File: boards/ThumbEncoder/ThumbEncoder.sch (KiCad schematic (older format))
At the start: 7 parts, among them P1 CONN_5X2, P2 CONN_5X2, P3 CONN_5X2, P4 CONN_1

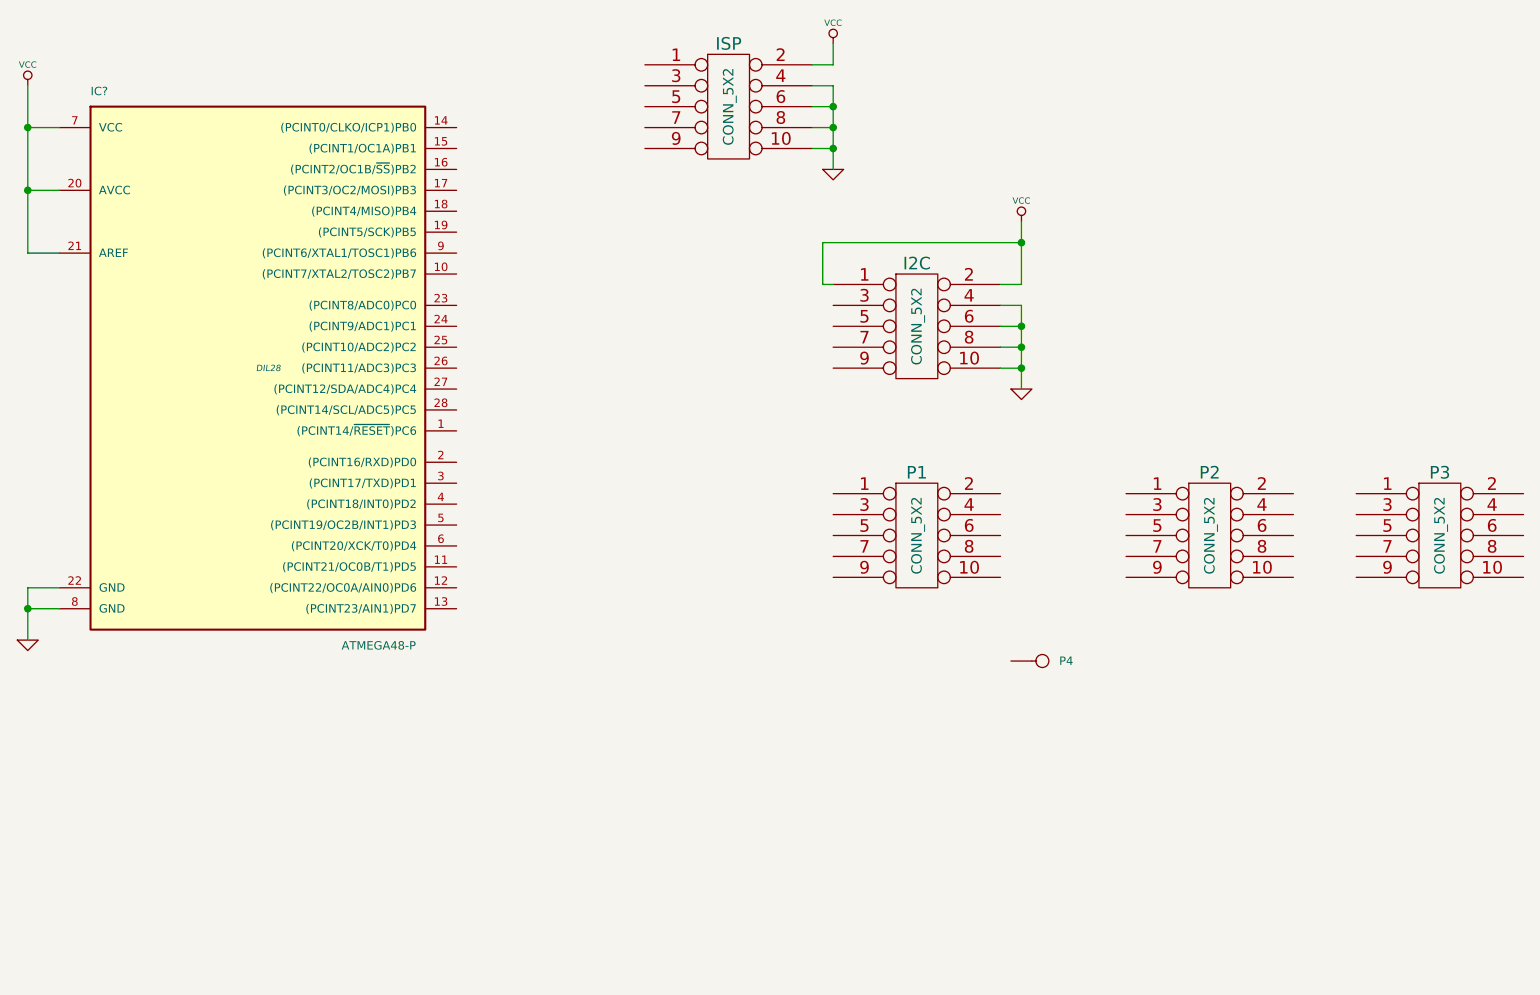
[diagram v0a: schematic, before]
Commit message: First version of thumb encoder schematics
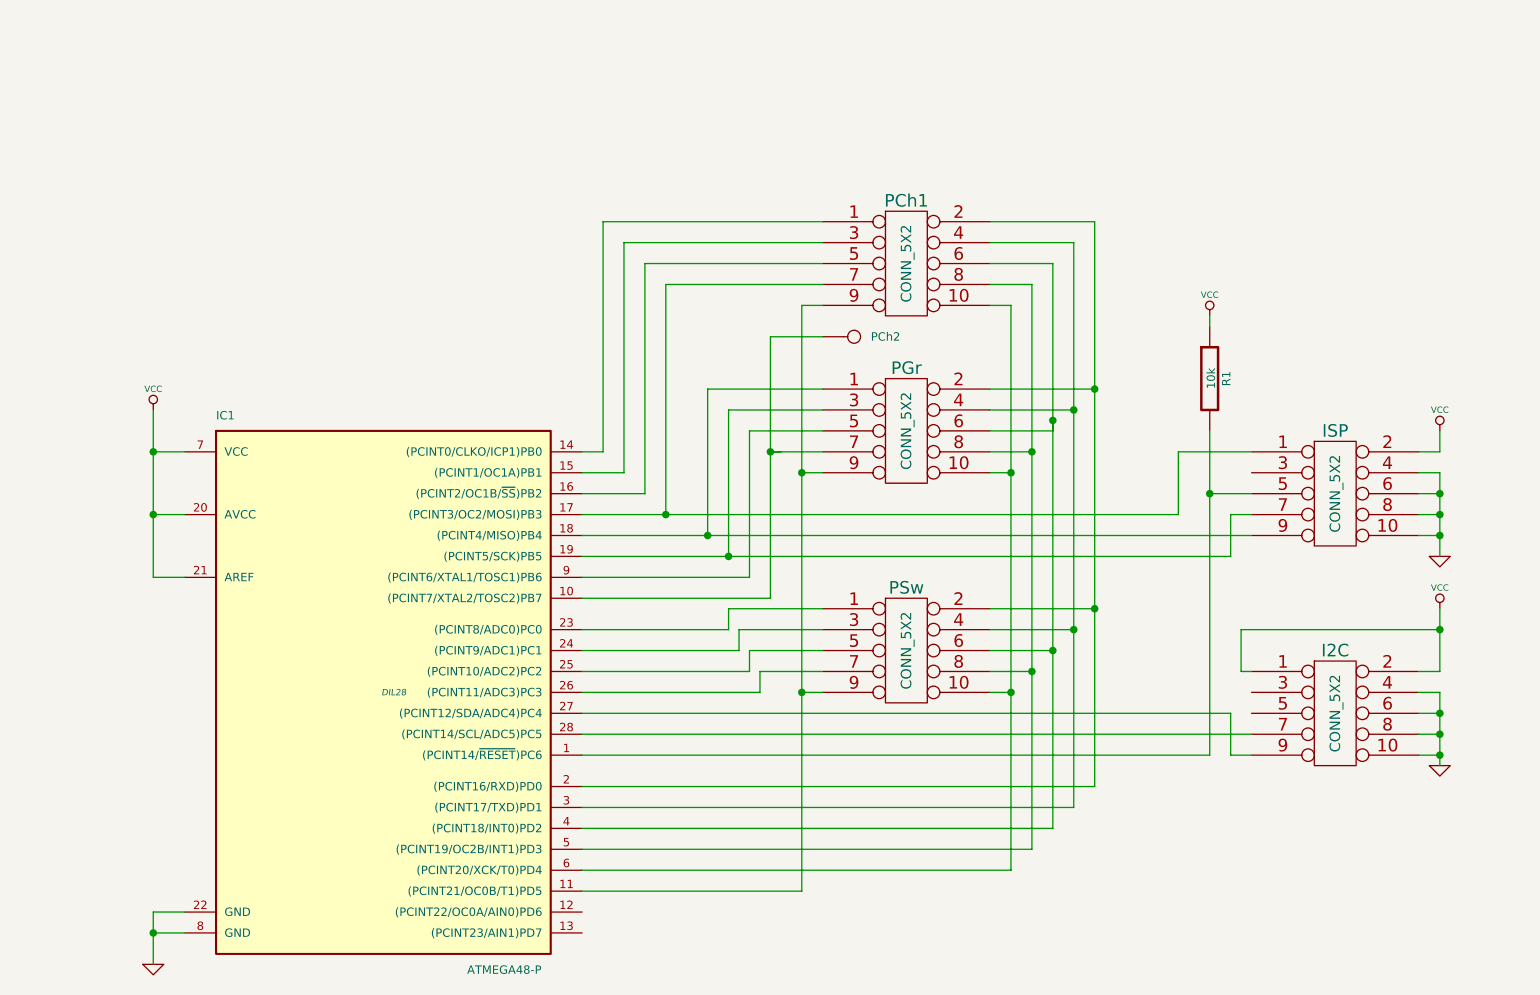
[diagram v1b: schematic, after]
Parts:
- added R1: 10k, ~, symbol R
- gave numbers to parts that had none: 1
- renumbered P1 to PCh1, P4 to PCh2, P2 to PGr, P3 to PSw
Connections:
- net VCC: now also R1.1
- net at IC1.1 ((PCINT14/~RESET~)PC6): now also ISP.5, R1.2
- net at IC1.10 ((PCINT7/XTAL2/TOSC2)PB7): now also PCh2.1, PGr.7
- net at IC1.11 ((PCINT21/OC0B/T1)PD5): now also PCh1.9, PGr.9, PSw.9
- net at IC1.14 ((PCINT0/CLKO/ICP1)PB0): now also PCh1.1
- net at IC1.15 ((PCINT1/OC1A)PB1): now also PCh1.3
- net at IC1.16 ((PCINT2/OC1B/~SS~)PB2): now also PCh1.5
- net at IC1.17 ((PCINT3/OC2/MOSI)PB3): now also ISP.1, PCh1.7
- net at IC1.18 ((PCINT4/MISO)PB4): now also ISP.9, PGr.1
- net at IC1.19 ((PCINT5/SCK)PB5): now also ISP.7, PGr.3
- net at IC1.2 ((PCINT16/RXD)PD0): now also PCh1.2, PGr.2, PSw.2
- net at IC1.23 ((PCINT8/ADC0)PC0): now also PSw.1
- net at IC1.24 ((PCINT9/ADC1)PC1): now also PSw.3
- net at IC1.25 ((PCINT10/ADC2)PC2): now also PSw.5
- net at IC1.26 ((PCINT11/ADC3)PC3): now also PSw.7
- net at IC1.27 ((PCINT12/SDA/ADC4)PC4): now also I2C.9
- net at IC1.28 ((PCINT14/SCL/ADC5)PC5): now also I2C.7
- net at IC1.3 ((PCINT17/TXD)PD1): now also PCh1.4, PGr.4, PSw.4
- net at IC1.4 ((PCINT18/INT0)PD2): now also PCh1.6, PGr.6, PSw.6
- net at IC1.5 ((PCINT19/OC2B/INT1)PD3): now also PCh1.8, PGr.8, PSw.8
- net at IC1.6 ((PCINT20/XCK/T0)PD4): now also PCh1.10, PGr.10, PSw.10
- net at IC1.9 ((PCINT6/XTAL1/TOSC1)PB6): now also PGr.5
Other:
- moved on the sheet: I2C, IC1, ISP, PCh1, PCh2, PGr, PSw
